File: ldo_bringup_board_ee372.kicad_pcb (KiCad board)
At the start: 4 copper layers, 100 x 100 mm, 152 parts, among them J1 VIN, J10 MD_SW_EN, J11 MD_MCU_PU_EN, J12 BUF_EN, J13 VSIG, J14 VSIG_BUF, J15 NR, J16 NOISE_X100, J17 NOISE_X1000, J18 VIN_PROBE, J19 VREF_PROBE, J2 GND, J20 VOUT_PROBE, J21 VG0_PROBE, J22 VG1_PROBE, J23 VG2_PROBE, J24 VG3_PROBE, J25 VG4_PROBE, J3 IBIAS, J4 VOUT, J5 VIN_SMA, J6 VOUT_SMA, J7 GND, J8 5V, J9 MD_MCU_EN, Q1 FDV305N, Q2 FDV305N, Q3 FDV305N, Q4 FDV305N, Q5 FDV305N, Q6 FDV305N, SW1 MD_SW, U1 LDO_DualMode_BGR_EE372, U2 Teensy4.1, U3 INA190A5IDDFR, U4 INA190A5IDDFR, U5 OPA4388IDR, U6 BUF602ID, U7 ADT7310TRZ

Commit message: Add first silkscreen items: logo, board title and names
- LOGO footprint on F.Silkscreen, 5.7 x 8.5 mm, marked not in
  schematic and excluded from the BOM and position files
- Board text: "EE372B LDO Bringup PCB", an underline, and the four
  author names
- Small routing edits: 796 track segments and 128 vias, up from 786
  and 127

DRC: 0 errors, 0 unconnected items, 0 schematic parity issues, 137
silkscreen warnings. Most of the silkscreen is still to do.
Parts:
- added G***: LOGO, LOGO, F.Cu at (111.2, 97.0)
- moved TP5 5.15 mm to (110.5, 89.0)
- moved C26 0.25 mm to (117.0, 104.0)
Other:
- board text added: "EE372B LDO Bringup PCB"
- board text added: "Luke Qiao Luis Sanchez Caleb Ketchum Spencer Wallace"
- board text added: "__________________________"

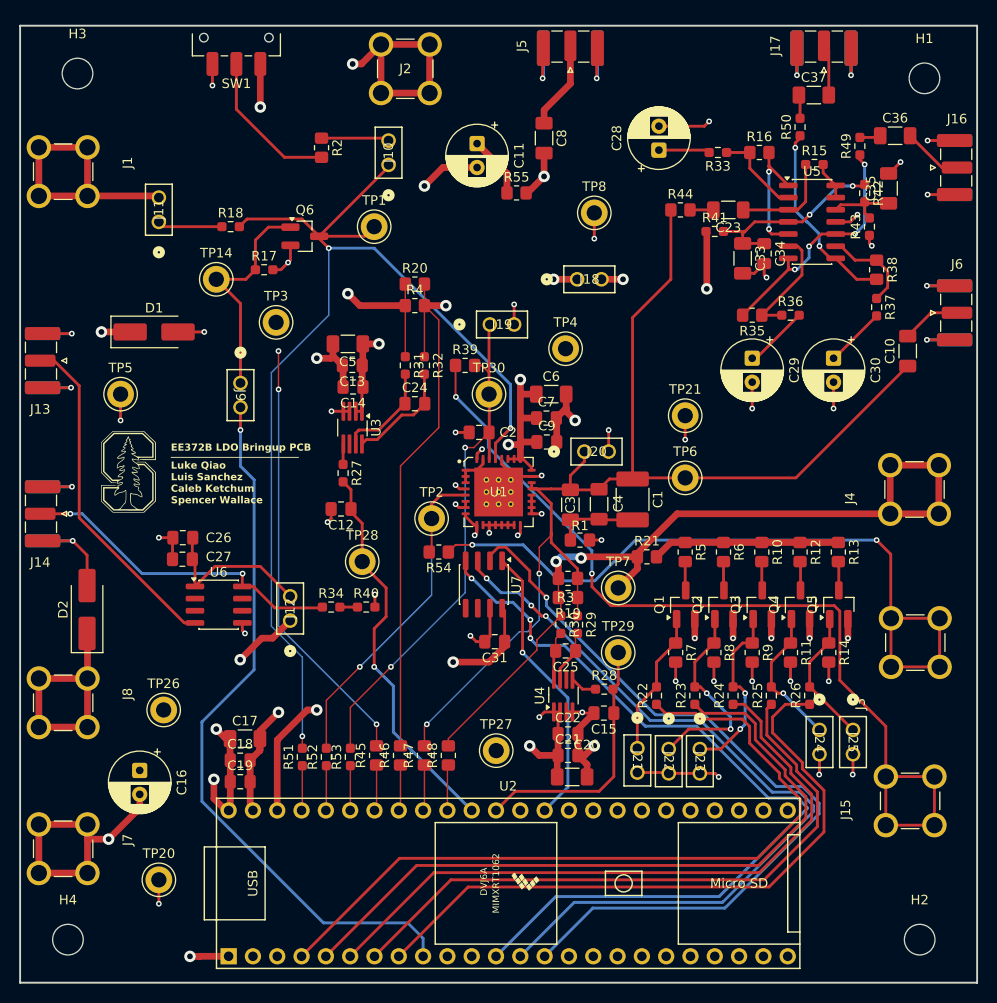
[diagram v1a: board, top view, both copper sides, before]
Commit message: Move C11 to VDD, remove R55, widen the analog tracks
Schematic: R55 removed. C11 pin 1 moves from VDD_LDO (through R55) to VDD,
the J1 side of R4. 151 parts, 109 nets, ERC 0 errors.

PCB:
- C11 moved to (114.5, 59.75), R55 footprint removed
- VOUT_LDO widened from 0.3 to 0.7 mm
- VSIG and VSIG_BUF widened from 0.3 to 0.6 mm, the R34 to R40 link and
  the R40 stub onto VDD_LDO to 0.7 mm
- J6 output and the noise amplifier input, outputs, stage links, supply
  and 2.5 V reference widened from 0.3 to 0.6 or 0.7 mm
- U3 sense tracks from R4 to R31 and R32 rerouted as a pair, R20 to R4
  links widened from 0.15 to 0.7 mm
- J12 moved to (126.25, 117.75), TP4 to (159.25, 83.0), R29 0.25 mm left
- VDD_LDO and +3V3 pour outlines on In2.Cu adjusted

DRC 0 errors, 0 unconnected, schematic parity 0.
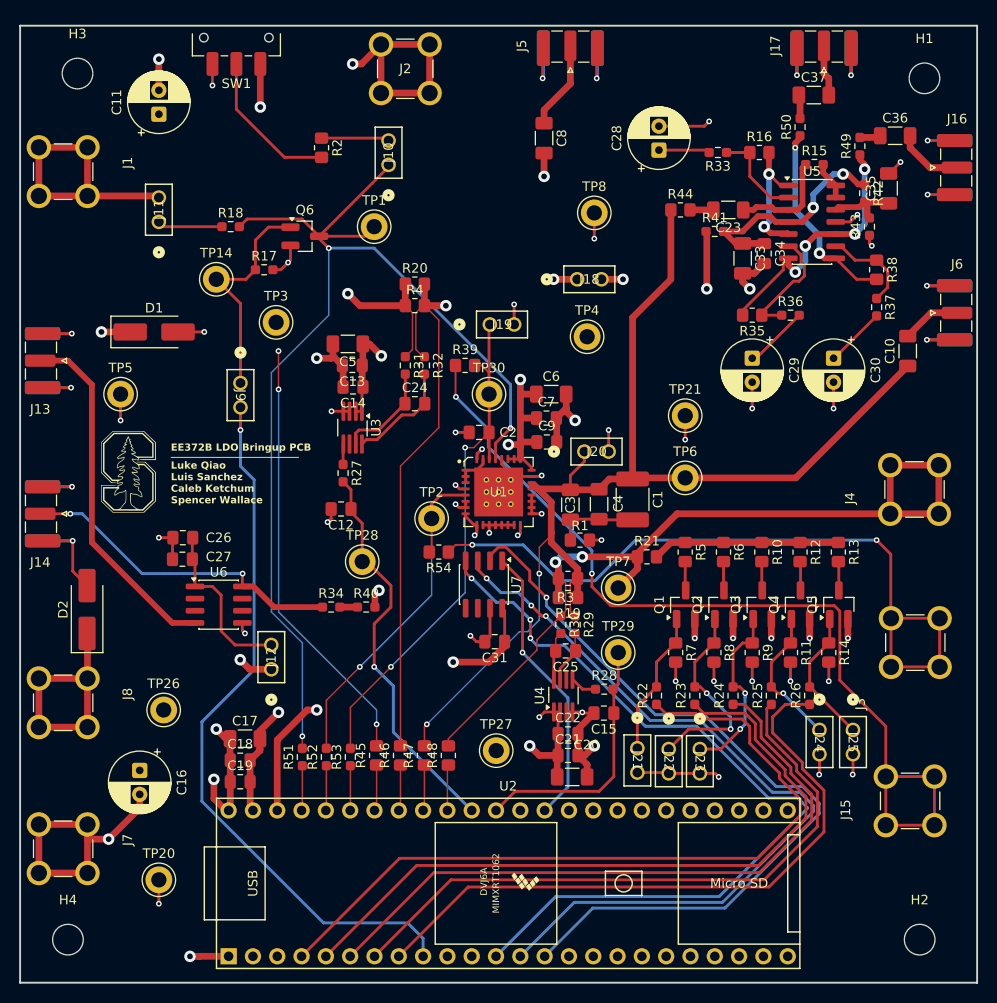
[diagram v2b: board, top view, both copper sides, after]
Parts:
- removed R55: 0, Resistor_SMD:R_0805_2012Metric_Pad1.20x1.40mm_HandSolder
- moved C11 33.4 mm to (114.5, 59.8), turned to 90 degrees
- moved J12 5.45 mm to (126.2, 117.8)
- moved TP4 2.57 mm to (159.2, 83.0)
- moved R29 0.25 mm to (158.0, 113.1)
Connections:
- C11 pad 1: Net-(C11-Pad1) -> SHUNT_IN_A
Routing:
- net Net-(C11-Pad1): track 6.45 -> 0.00 mm
- net SHUNT_OUT_B: track 86.5 -> 90.4 mm
- net Net-(U5E-V+): track 20.4 -> 24.0 mm
- net +5V: track 51.5 -> 48.2 mm
- net GND: track 293.7 -> 291.0 mm
- net Net-(U5B-+): track 13.3 -> 15.6 mm
- net VSIG: track 35.6 -> 37.2 mm
- net SHUNT_OUT_A: track 124.8 -> 126.4 mm
- net Net-(U5C-+): track 26.0 -> 27.5 mm
- net SHUNT_IN_B: track 92.1 -> 90.7 mm
- net +3V3: track 45.1 -> 45.9 mm
- net Net-(C36-Pad2): track 6.28 -> 7.01 mm
- net /MCU Conn/ISENSE_IN: track 40.9 -> 41.6 mm
- net SHUNT_IN_A: track 95.3 -> 95.9 mm
- net Net-(U6-V+): track 17.6 -> 18.2 mm

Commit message: Layout: move the left-edge connectors, mounting holes and TP20
- J1, J7, J8 banana jacks and the J13, J14 SMAs moved along the left edge
- J2 moved 3 mm left, D2 and C16 moved, TP20 (GND) moved to (115, 116.5)
- Mounting holes now at (105.25, 55), (194.75, 55), (105.25, 146) and
  (194.75, 146)
- VSIG and VSIG_BUF rerouted to the moved SMAs
- Top-layer GND tracks between the J2 and J7 jack pins removed, the pins
  connect through the In1 plane
- +5V and VDD pour outlines on In2.Cu adjusted

Schematic unchanged. DRC 0 errors, 0 unconnected, schematic parity 0.
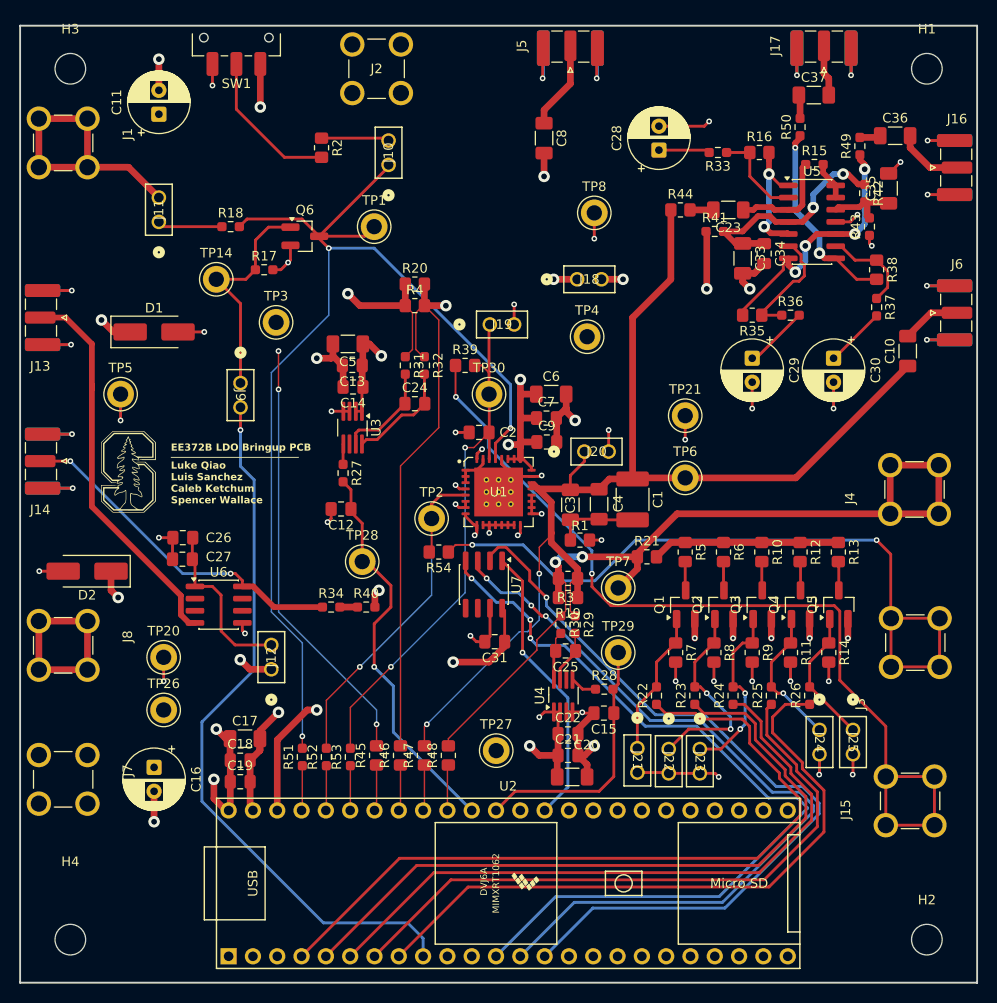
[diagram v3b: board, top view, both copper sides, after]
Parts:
- moved TP20 23.3 mm to (115.0, 116.5)
- moved J7 7.25 mm to (104.5, 129.2)
- moved J8 6.00 mm to (104.5, 115.2)
- moved J14 5.50 mm to (102.1, 96.0)
- moved J13 4.50 mm to (102.1, 81.0)
- moved D2 4.00 mm to (107.0, 107.5), turned to 180 degrees
- moved J1 3.00 mm to (104.5, 62.8)
- moved J2 3.00 mm to (137.2, 55.0)
- moved C16 1.53 mm to (114.0, 128.0)
- moved H1 1.03 mm to (194.8, 55.0)
- moved H3 0.90 mm to (105.2, 55.0)
- moved H2 0.75 mm to (194.8, 146.0)
- moved H4 0.25 mm to (105.2, 146.0)
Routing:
- net GND: track 291.0 -> 233.2 mm, vias 62 -> 61
- net VSIG: track 37.2 -> 41.0 mm
- net VSIG_BUF: track 34.5 -> 36.3 mm
- net SHUNT_IN_A: track 95.9 -> 97.7 mm
- net +5V: track 48.2 -> 46.6 mm, vias 4 -> 5

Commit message: Checkpoint: add GND pours on F.Cu and B.Cu
- GND zone on F.Cu and on B.Cu, each covering the board 0.5 mm inside the
  edge, 0.5 mm clearance
- TP2 (IBIAS) moved 0.75 mm, IBIAS and nearby GND tracks rerouted

No stitching vias added yet. Schematic unchanged.
DRC 0 errors, 0 unconnected, schematic parity 0.
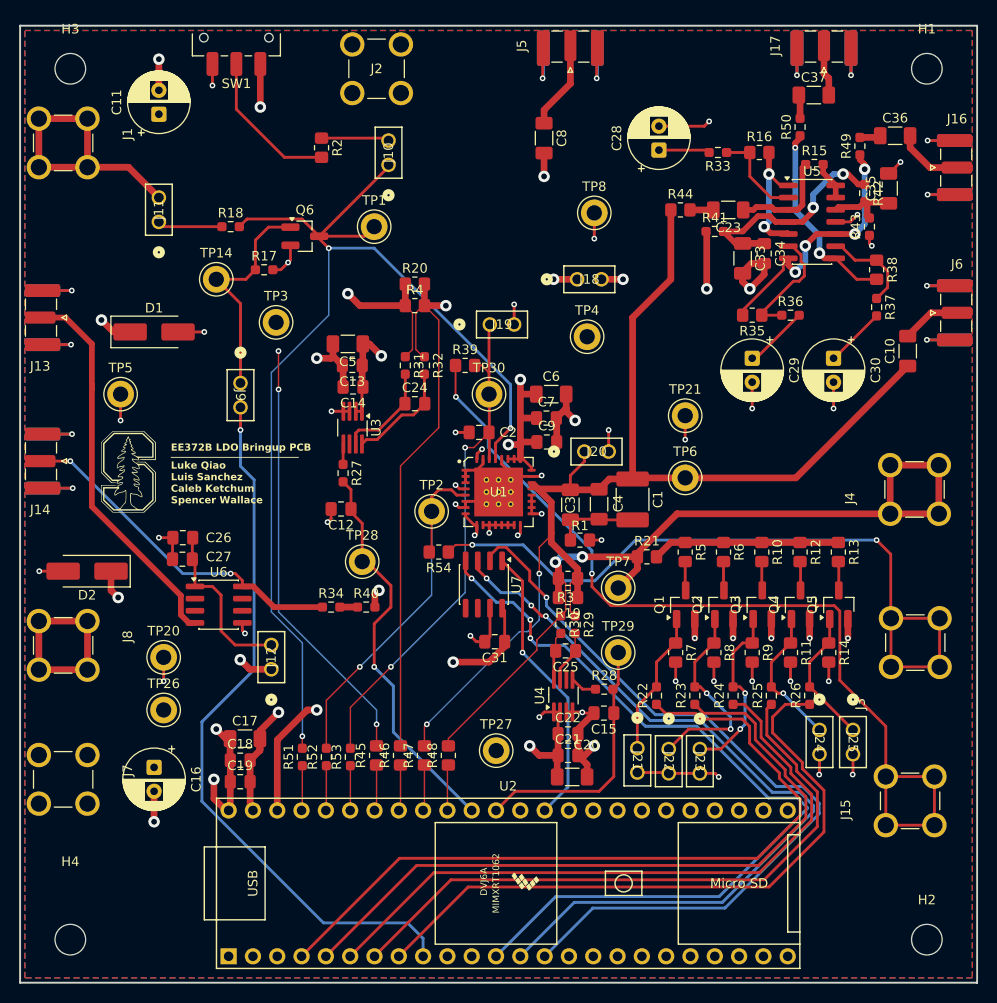
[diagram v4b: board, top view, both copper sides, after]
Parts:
- moved TP2 0.75 mm to (143.0, 101.2)
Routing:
- net GND: track 233.2 -> 238.8 mm
- net IBIAS: track 37.5 -> 39.2 mm
- added copper zone on B.Cu, net GND
- added copper zone on F.Cu, net GND
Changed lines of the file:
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@@
 	(footprint "TestPoint:TestPoint_Keystone_5005-5009_Compact"
 		(layer "F.Cu")
-		(at 143 102)
+		(at 143 101.25)
 		(descr "Keystone THM Compact Test Point 5005-5009, http://www.keyelco.com/product-pdf.cfm?p=1314")
 		(tags "Through Hole Mount Test Points")
@@
 	)
 	(segment
+		(start 148.425 100.2)
+		(end 148.725 100.5)
+		(width 0.3)
+		(layer "F.Cu")
+		(net "GND")
+	)
+	(segment
 		(start 194.75 77.675)
 		(end 197.65 77.675)
@@
 	)
 	(segment
-		(start 176.725 76.375)
-		(end 177.75 75.35)
-		(width 0.7)
-		(layer "F.Cu")
-		(net "GND")
-	)
-	(segment
 		(start 168.5 117)
 		(end 168.5 119)
@@
 	)
 	(segment
-		(start 159.25 129)
-		(end 159.25 127.7125)
+		(start 146.55 100.2)
+		(end 148.425 100.2)
+		(width 0.3)
+		(layer "F.Cu")
+		(net "GND")
+	)
+	(segment
+		(start 177.75 76.5)
+		(end 176.25 78)
 		(width 0.7)
 		(layer "F.Cu")
@@
 	)
 	(segment
-		(start 157.0625 90.475)
-		(end 156.0375 91.5)
+		(start 159.25 129)
+		(end 159.25 127.7125)
 		(width 0.7)
 		(layer "F.Cu")
@@
 	)
 	(segment
-		(start 175.5 76.375)
-		(end 176.725 76.375)
+		(start 157.0625 90.475)
+		(end 156.0375 91.5)
 		(width 0.7)
 		(layer "F.Cu")
@@
 	)
 	(segment
+		(start 176.4 75.35)
+		(end 177.75 75.35)
+		(width 0.7)
+		(layer "F.Cu")
+		(net "GND")
+	)
+	(segment
 		(start 148.375 96.294542)
 		(end 147.719542 96.95)
@@
 	)
 	(segment
+		(start 175.5 76.25)
+		(end 176.4 75.35)
+		(width 0.7)
+		(layer "F.Cu")
+		(net "GND")
+	)
+	(segment
 		(start 158.83 122.33)
 		(end 159.965 122.33)
@@
 	)
 	(segment
+		(start 175.5 76.375)
+		(end 175.5 76.25)
+		(width 0.7)
+		(layer "F.Cu")
+		(net "GND")
+	)
+	(segment
 		(start 176.5 87.75)
 		(end 176.5 90.5)
@@
 	)
 	(segment
+		(start 177.75 75.35)
+		(end 177.75 76.5)
+		(width 0.7)
+		(layer "F.Cu")
+		(net "GND")
+	)
+	(segment
 		(start 158.2875 126.75)
 		(end 158.2875 124.5)
@@
 	)
 	(segment
-		(start 135.5 117.5)
-		(end 132 121)
-		(width 0.15)
+		(start 146.55 99.55)
+		(end 145.630761 99.55)
+		(width 0.3)
 		(layer "F.Cu")
 		(net "IBIAS")
 	)
 	(segment
-		(start 143 100.5)
-		(end 143 102.5)
+		(start 143.75 99)
+		(end 143 99.75)
 		(width 0.3)
 		(layer "F.Cu")
@@
 	)
 	(segment
-		(start 146.55 99.55)
-		(end 143.95 99.55)
+		(start 135.5 117.5)
+		(end 132 121)
+		(width 0.15)
+		(layer "F.Cu")
+		(net "IBIAS")
+	)
+	(segment
+		(start 145.080761 99)
+		(end 143.75 99)
 		(width 0.3)
 		(layer "F.Cu")
@@
 	)
 	(segment
-		(start 143.95 99.55)
-		(end 143 100.5)
+		(start 143 99.75)
+		(end 143 102.5)
 		(width 0.3)
 		(layer "F.Cu")
@@
 	)
 	(segment
-		(start 142.75 102.75)
-		(end 143 102.5)
-		(width 0.2)
+		(start 145.630761 99.55)
+		(end 145.080761 99)
+		(width 0.3)
 		(layer "F.Cu")
 		(net "IBIAS")
@@
 	)
 	(segment
-		(start 143 110)
-		(end 143 102.5)
+		(start 135.5 117.5)
+		(end 143 110)
 		(width 0.15)
 		(layer "B.Cu")
@@
 	)
 	(segment
-		(start 135.5 117.5)
-		(end 143 110)
+		(start 143 110)
+		(end 143 101.25)
 		(width 0.15)
 		(layer "B.Cu")
@@
 	)
 	(zone
+		(net "GND")
+		(layer "F.Cu")
+		(name "Ground_L1")
+		(hatch edge 0.5)
+		(connect_pads
+			(clearance 0.5)
+		)
+		(min_thickness 0.25)
+		(fill yes
+			(thermal_gap 0.5)
+			(thermal_bridge_width 0.5)
+			(island_removal_mode 0)
+		)
+		(polygon
+			(pts
+				(xy 100.5 51) (xy 199.5 51) (xy 199.5 150) (xy 100.5 150)
+			)
+		)
+	)
+	(zone
+		(net "GND")
+		(layer "B.Cu")
+		(name "Ground_L4")
+		(hatch edge 0.5)
+		(connect_pads
+			(clearance 0.5)
+		)
+		(min_thickness 0.25)
+		(fill yes
+			(thermal_gap 0.5)
+			(thermal_bridge_width 0.5)
+			(island_removal_mode 0)
+		)
+		(polygon
+			(pts
+				(xy 100.5 51) (xy 199.5 51) (xy 199.5 150) (xy 100.5 150)
+			)
+		)
+	)
+	(zone
